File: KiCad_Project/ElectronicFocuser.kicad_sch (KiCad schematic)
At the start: 4 parts, among them J1 JST-XH Stepper Motor, U1 ULN2003

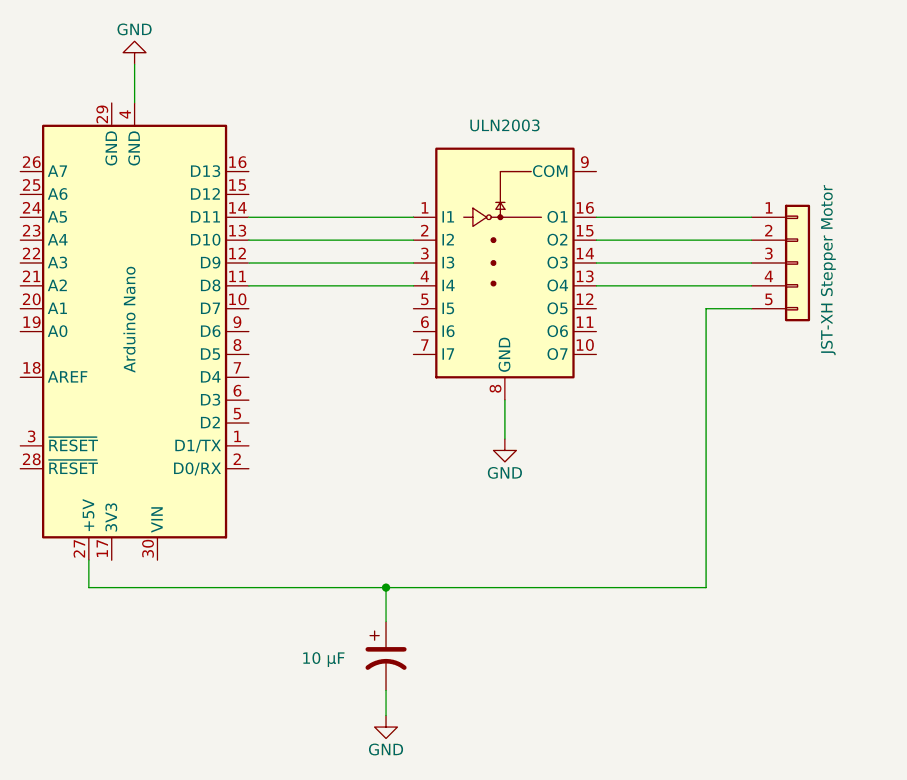
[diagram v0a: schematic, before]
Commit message: Forgot to connect pin 9 of ULN2003, which could cause electrical issues due to EMF
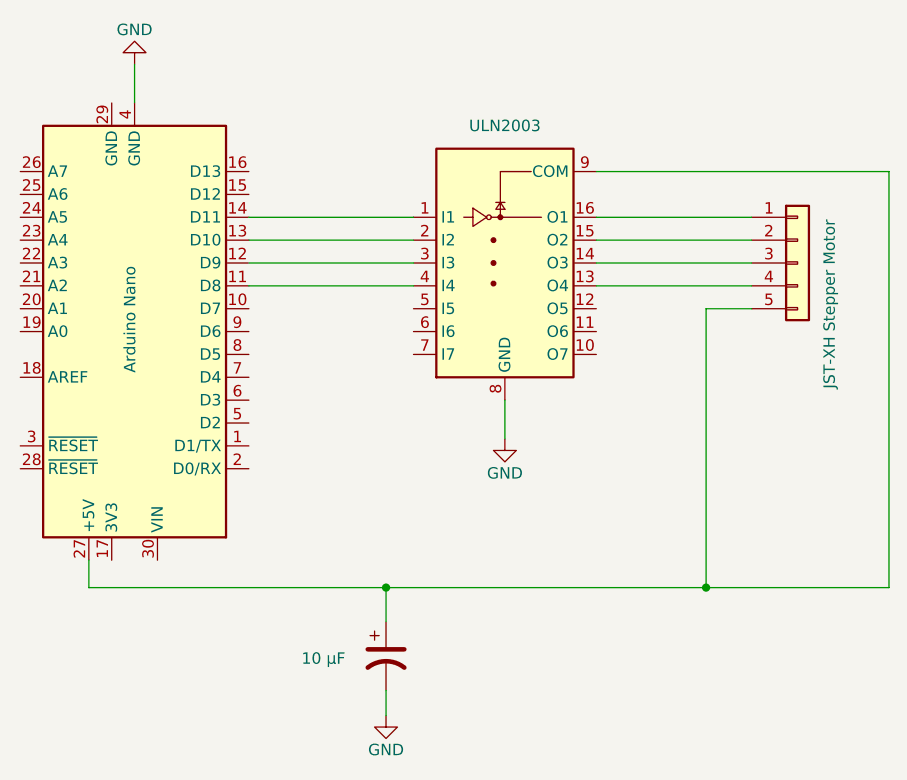
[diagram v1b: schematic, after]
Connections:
- net at U1.9 (COM): now also A1.27 (+5V), C1.1, J1.5 (Pin_5)
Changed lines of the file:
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@@
     (comment 4 "Author: Julien Lecomte")
   )
+  (junction (at 175.26 117.348) (diameter 0) (color 0 0 0 0)
+  )
   (junction (at 139.7 117.348) (diameter 0) (color 0 0 0 0)
+  )
+  (wire (pts (xy 195.58 71.12) (xy 195.58 117.348))
+    (stroke (width 0) (type default) (color 0 0 0 0))
   )
   (wire (pts (xy 124.46 78.74) (xy 142.748 78.74))
@@
     (stroke (width 0) (type default) (color 0 0 0 0))
   )
+  (wire (pts (xy 195.58 117.348) (xy 175.26 117.348))
+    (stroke (width 0) (type default) (color 0 0 0 0))
+  )
   (wire (pts (xy 124.46 83.82) (xy 142.748 83.82))
     (stroke (width 0) (type default) (color 0 0 0 0))
@@
   )
   (wire (pts (xy 175.26 117.348) (xy 175.26 86.36))
+    (stroke (width 0) (type default) (color 0 0 0 0))
+  )
+  (wire (pts (xy 163.068 71.12) (xy 195.58 71.12))
     (stroke (width 0) (type default) (color 0 0 0 0))
   )
@@
       (effects (font (size 1.27 1.27)) (justify left) hide)
     )
-    (property "Value" "JST-XH Stepper Motor" (id 1) (at 188.722 91.44 90)
+    (property "Value" "JST-XH Stepper Motor" (id 1) (at 188.976 95.25 90)
       (effects (font (size 1.27 1.27)) (justify left))
     )
